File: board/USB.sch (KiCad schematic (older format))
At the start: 47 parts, among them J1 USB_MICRO_B, J7 USB_MICRO_B, P11 CONN_1, P12 CONN_1, P13 CONN_1, U18 USB3340, U2 CY7C68013A_100AC, U24 BDXXGA5WEFJ_, X1 CRYSTAL

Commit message: Issue #1605
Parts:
- added P? (x2): CONN_5, symbol CONN_5
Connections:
- wire segments 176 -> 189
- no-connect marks 5 -> 7
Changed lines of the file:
@@
 Sheet 9 12
 Title "HDMI2USB"
-Date "11 mar 2015"
+Date "12 mar 2015"
 Rev "Rev2"
 Comp ""
@@
 	1    0    0    -1
 $EndComp
-Text Label 14900 3950 0    60   ~ 0
+Text Label 14600 3950 0    60   ~ 0
 CYDP
 Text Label 12000 4050 2    60   ~ 0
@@
 0D 08 60 00 00 34 20 80 01 00 D0 80 00 06 00 40 03 02 18 00 00 0D 08 60 00 00 34 20 80 01 00 D0
 80 00 06 00 40 03 02 18 00 00 0D FE 0D 6E A0 C3 78 63 AE 4C 0B 00 00 00 00 49 45 4E 44 AE 42 60
-82 00 $EndBitmap
+82 06 $EndBitmap
 EndData
 $EndBitmap
-$Comp
-L PWR_FLAG #FLG039
-U 1 1 54AFC1D5
-P 14850 3500
-F 0 "#FLG039" H 14850 3595 30  0001 C CNN
-F 1 "PWR_FLAG" H 14850 3680 30  0000 C CNN
-F 2 "" H 14850 3500 60  0000 C CNN
-F 3 "" H 14850 3500 60  0000 C CNN
-	1    14850 3500
-	1    0    0    -1
-$EndComp
 $Comp
 L USB3340 U18
@@
 Text Label 12000 4150 2    60   ~ 0
 CYDP
-Text Label 14900 3850 0    60   ~ 0
+Text Label 14600 3850 0    60   ~ 0
 CYDN
 Text Label 12400 1450 2    60   ~ 0
@@
 Text Label 3900 8750 2    60   ~ 0
 USB_DM
-Text Label 5350 8800 0    60   ~ 0
+Text Label 5150 8800 0    60   ~ 0
 USB_DP
-Text Label 5350 8900 0    60   ~ 0
+Text Label 5150 8900 0    60   ~ 0
 USB_DM
 NoConn ~ 3500 10500
@@
 	1    0    0    -1
 $EndComp
-Text Label 5350 9000 0    60   ~ 0
+Text Label 5150 9000 0    60   ~ 0
 USB_5V
 $Comp
@@
 Connection ~ 12750 9700
 Wire Wire Line
-	14900 3950 15100 3950
-Wire Wire Line
-	15100 3850 14900 3850
+	14600 3950 15100 3950
+Wire Wire Line
+	14600 3850 15100 3850
 Wire Wire Line
 	14500 6000 14100 6000
@@
 	13250 1650 15350 1650
 Wire Wire Line
-	14850 3500 14850 3750
-Connection ~ 14850 3750
-Wire Wire Line
 	5350 8600 5700 8600
 Wire Wire Line
@@
 Text Notes 12150 8850 0    118  ~ 24
 Cypress CY7C68013A\nDecoupling Capacitors
+$Comp
+L CONN_5 P?
+U 1 1 5501BEC3
+P 15500 3300
+F 0 "P?" V 15450 3300 50  0000 C CNN
+F 1 "CONN_5" V 15550 3300 50  0000 C CNN
+F 2 "" H 15500 3300 60  0000 C CNN
+F 3 "" H 15500 3300 60  0000 C CNN
+	1    15500 3300
+	1    0    0    -1
+$EndComp
+$Comp
+L CONN_5 P?
+U 1 1 5501BED0
+P 6150 9500
+F 0 "P?" V 6100 9500 50  0000 C CNN
+F 1 "CONN_5" V 6200 9500 50  0000 C CNN
+F 2 "" H 6150 9500 60  0000 C CNN
+F 3 "" H 6150 9500 60  0000 C CNN
+	1    6150 9500
+	1    0    0    -1
+$EndComp
+Wire Wire Line
+	5650 9000 5650 9300
+Wire Wire Line
+	5650 9300 5750 9300
+Connection ~ 5650 9000
+Wire Wire Line
+	5600 8900 5600 9400
+Wire Wire Line
+	5600 9400 5750 9400
+Connection ~ 5600 8900
+Wire Wire Line
+	5550 8800 5550 9500
+Wire Wire Line
+	5550 9500 5750 9500
+Connection ~ 5550 8800
+Text Label 5550 9600 0    60   ~ 0
+GND
+Wire Wire Line
+	5550 9600 5750 9600
+NoConn ~ 5750 9700
+NoConn ~ 15100 3500
+Wire Wire Line
+	14750 3750 14750 3100
+Wire Wire Line
+	14750 3100 15100 3100
+Connection ~ 14750 3750
+Text Label 14950 3400 0    60   ~ 0
+GND
+Wire Wire Line
+	14950 3400 15100 3400
+Wire Wire Line
+	15100 3200 14850 3200
+Wire Wire Line
+	14850 3200 14850 3850
+Connection ~ 14850 3850
+Wire Wire Line
+	14900 3950 14900 3300
+Wire Wire Line
+	14900 3300 15100 3300
+Connection ~ 14900 3950
 $EndSCHEMATC

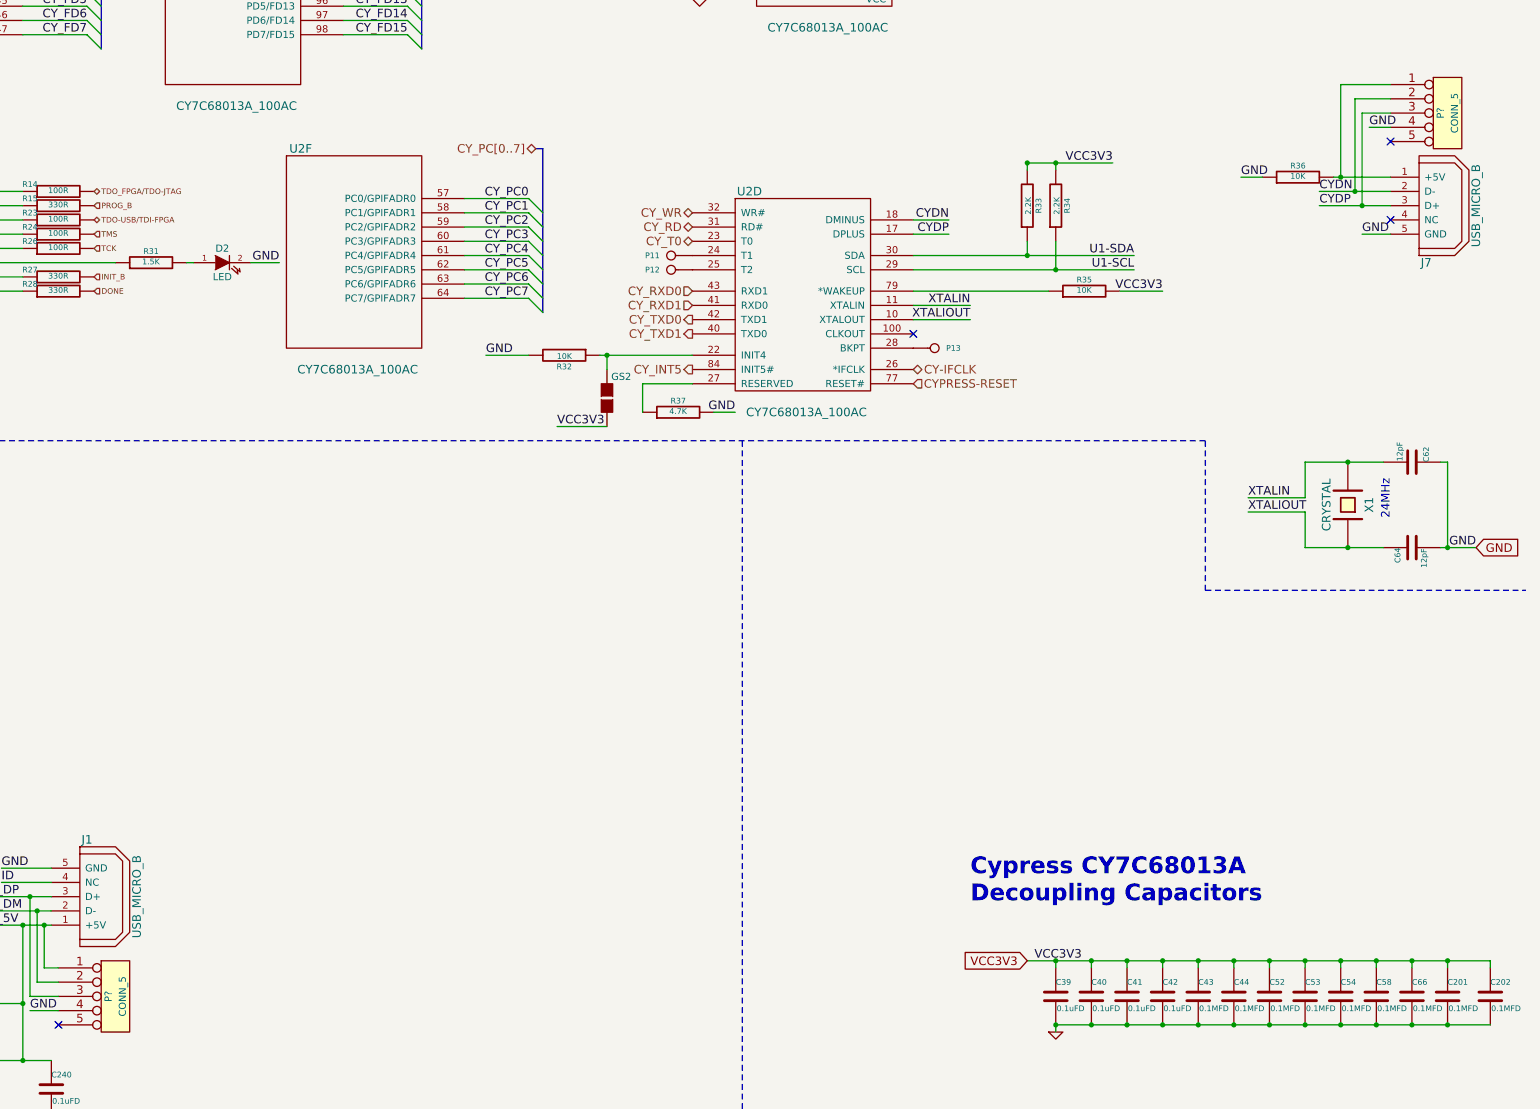
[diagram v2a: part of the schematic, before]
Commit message: Issue #1680 - Bank 0 Ios
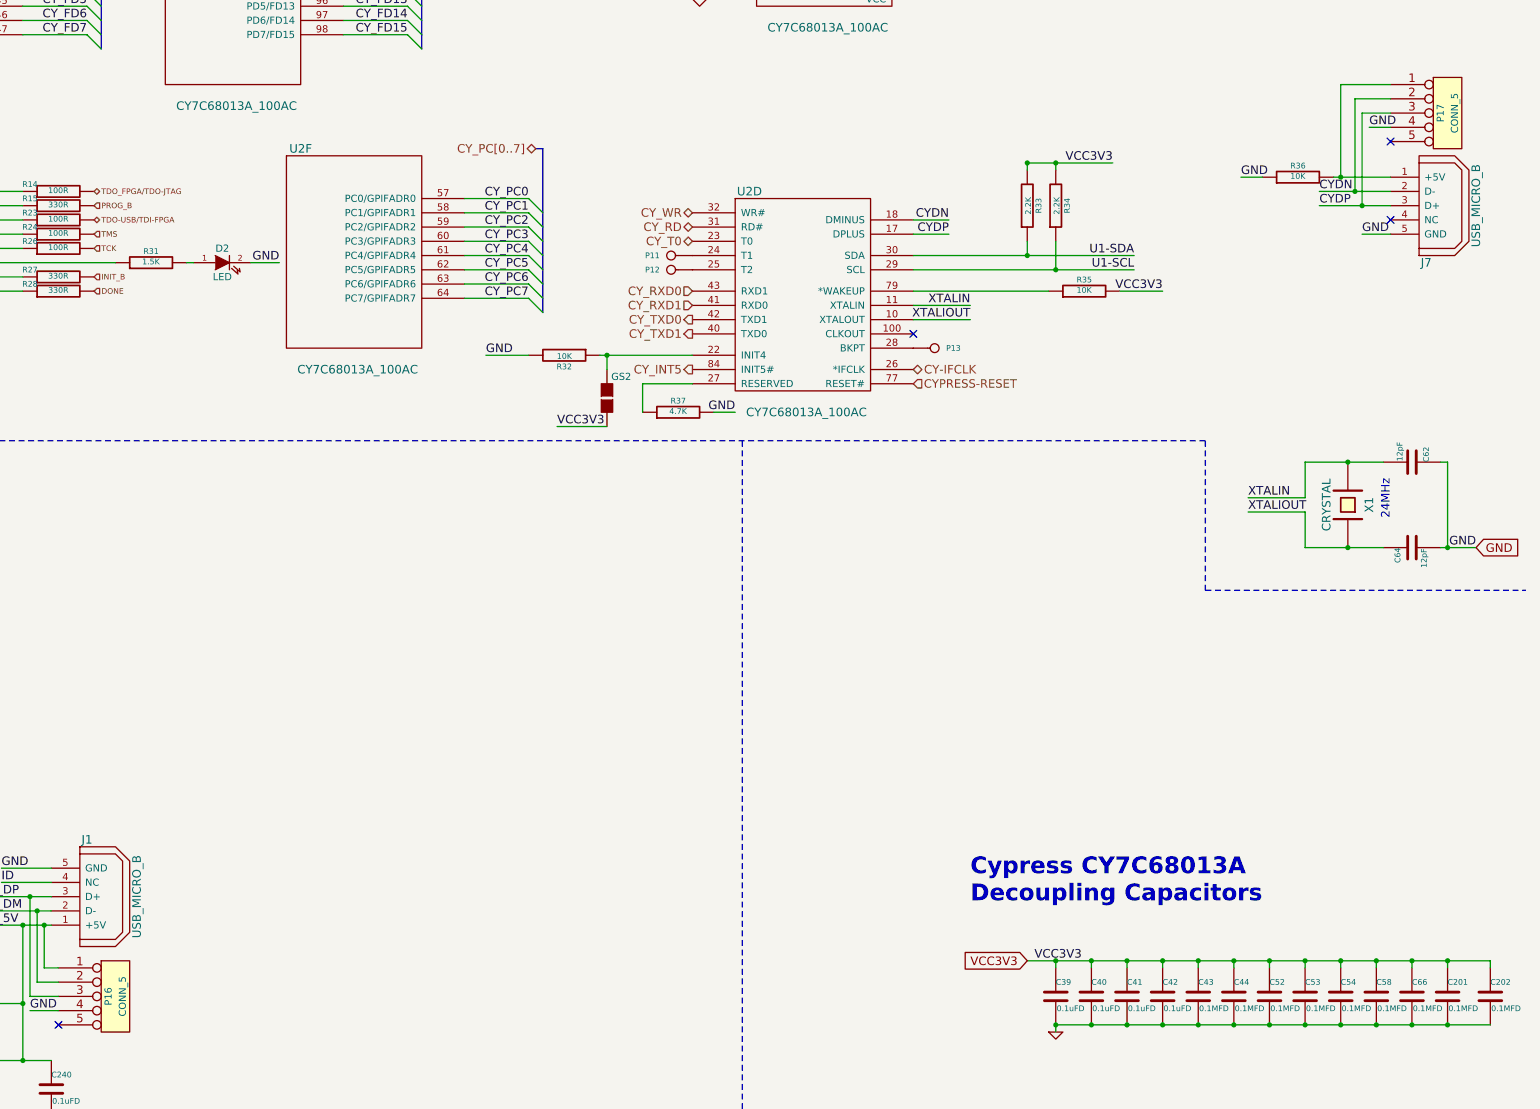
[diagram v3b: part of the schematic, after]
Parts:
- gave numbers to parts that had none: 2
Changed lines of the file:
@@
 $Descr A3 16535 11693
 encoding utf-8
-Sheet 9 12
+Sheet 12 12
 Title "HDMI2USB"
-Date "12 mar 2015"
+Date "23 mar 2015"
 Rev "Rev2"
 Comp ""
@@
 $EndComp
 $Comp
-L GND #PWR038
+L GND #PWR044
 U 1 1 54AFC1CB
 P 12750 9750
-F 0 "#PWR038" H 12750 9750 30  0001 C CNN
+F 0 "#PWR044" H 12750 9750 30  0001 C CNN
 F 1 "GND" H 12750 9680 30  0001 C CNN
 F 2 "" H 12750 9750 60  0000 C CNN
@@
 0D 08 60 00 00 34 20 80 01 00 D0 80 00 06 00 40 03 02 18 00 00 0D 08 60 00 00 34 20 80 01 00 D0
 80 00 06 00 40 03 02 18 00 00 0D FE 0D 6E A0 C3 78 63 AE 4C 0B 00 00 00 00 49 45 4E 44 AE 42 60
-82 06 $EndBitmap
+82 02 $EndBitmap
 EndData
 $EndBitmap
@@
 VCC3V3
 $Comp
-L GND #PWR040
+L GND #PWR045
 U 1 1 54AFC1E5
 P 10250 2500
-F 0 "#PWR040" H 10250 2500 30  0001 C CNN
+F 0 "#PWR045" H 10250 2500 30  0001 C CNN
 F 1 "GND" H 10250 2430 30  0001 C CNN
 F 2 "" H 10250 2500 60  0000 C CNN
@@
 USB_5V
 $Comp
-L GND #PWR041
+L GND #PWR046
 U 1 1 54E5E8EF
 P 2500 11000
-F 0 "#PWR041" H 2500 11000 30  0001 C CNN
+F 0 "#PWR046" H 2500 11000 30  0001 C CNN
 F 1 "GND" H 2500 10930 30  0001 C CNN
 F 2 "" H 2500 11000 60  0000 C CNN
@@
 Cypress CY7C68013A\nDecoupling Capacitors
 $Comp
-L CONN_5 P?
+L CONN_5 P17
 U 1 1 5501BEC3
 P 15500 3300
-F 0 "P?" V 15450 3300 50  0000 C CNN
+F 0 "P17" V 15450 3300 50  0000 C CNN
 F 1 "CONN_5" V 15550 3300 50  0000 C CNN
 F 2 "" H 15500 3300 60  0000 C CNN
@@
 $EndComp
 $Comp
-L CONN_5 P?
+L CONN_5 P16
 U 1 1 5501BED0
 P 6150 9500
-F 0 "P?" V 6100 9500 50  0000 C CNN
+F 0 "P16" V 6100 9500 50  0000 C CNN
 F 1 "CONN_5" V 6200 9500 50  0000 C CNN
 F 2 "" H 6150 9500 60  0000 C CNN

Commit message: Issue #1683
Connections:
- net U1-SCL renamed MAC_SCL
- net U1-SDA renamed MAC_SDA
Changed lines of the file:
@@
 $Descr A3 16535 11693
 encoding utf-8
-Sheet 12 12
+Sheet 11 12
 Title "HDMI2USB"
-Date "23 mar 2015"
+Date "25 mar 2015"
 Rev "Rev2"
 Comp ""
@@
 $EndComp
 $Comp
-L GND #PWR044
+L GND #PWR040
 U 1 1 54AFC1CB
 P 12750 9750
-F 0 "#PWR044" H 12750 9750 30  0001 C CNN
+F 0 "#PWR040" H 12750 9750 30  0001 C CNN
 F 1 "GND" H 12750 9680 30  0001 C CNN
 F 2 "" H 12750 9750 60  0000 C CNN
@@
 0D 08 60 00 00 34 20 80 01 00 D0 80 00 06 00 40 03 02 18 00 00 0D 08 60 00 00 34 20 80 01 00 D0
 80 00 06 00 40 03 02 18 00 00 0D FE 0D 6E A0 C3 78 63 AE 4C 0B 00 00 00 00 49 45 4E 44 AE 42 60
-82 02 $EndBitmap
+82 00 $EndBitmap
 EndData
 $EndBitmap
@@
 VCC3V3
 $Comp
-L GND #PWR045
+L GND #PWR041
 U 1 1 54AFC1E5
 P 10250 2500
-F 0 "#PWR045" H 10250 2500 30  0001 C CNN
+F 0 "#PWR041" H 10250 2500 30  0001 C CNN
 F 1 "GND" H 10250 2430 30  0001 C CNN
 F 2 "" H 10250 2500 60  0000 C CNN
@@
 USB_5V
 $Comp
-L GND #PWR046
+L GND #PWR042
 U 1 1 54E5E8EF
 P 2500 11000
-F 0 "#PWR046" H 2500 11000 30  0001 C CNN
+F 0 "#PWR042" H 2500 11000 30  0001 C CNN
 F 1 "GND" H 2500 10930 30  0001 C CNN
 F 2 "" H 2500 11000 60  0000 C CNN
@@
 	14900 3300 15100 3300
 Connection ~ 14900 3950
+Text HLabel 13300 4300 2    39   BiDi ~ 0
+MAC_SDA
+Text HLabel 13300 4400 2    39   Input ~ 0
+MAC_SCL
 $EndSCHEMATC

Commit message: Issue #1670
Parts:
- added P18: CONN_2, symbol CONN_2
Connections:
- net MAC_SDA: now also P18.2 (PM); no longer R33.1, U2.30 (SDA)
- new net U1-SDA: P18.1 (P1), R33.1, U2.30 (SDA)
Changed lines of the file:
@@
 $Descr A3 16535 11693
 encoding utf-8
-Sheet 11 12
+Sheet 10 12
 Title "HDMI2USB"
-Date "25 mar 2015"
+Date "30 mar 2015"
 Rev "Rev2"
 Comp ""
@@
 0D 08 60 00 00 34 20 80 01 00 D0 80 00 06 00 40 03 02 18 00 00 0D 08 60 00 00 34 20 80 01 00 D0
 80 00 06 00 40 03 02 18 00 00 0D FE 0D 6E A0 C3 78 63 AE 4C 0B 00 00 00 00 49 45 4E 44 AE 42 60
-82 00 $EndBitmap
+82 0E $EndBitmap
 EndData
 $EndBitmap
@@
 Text Notes 650  850  0    118  ~ 24
 USB 2.0 Device Port\nJTAG Programmer and "Easy" High Speed USB 2.0 Interface\nCypress FX2 based
+Text Notes 12150 8850 0    118  ~ 24
+Cypress CY7C68013A\nDecoupling Capacitors
+$Comp
+L CONN_5 P17
+U 1 1 5501BEC3
+P 15500 3300
+F 0 "P17" V 15450 3300 50  0000 C CNN
+F 1 "CONN_5" V 15550 3300 50  0000 C CNN
+F 2 "" H 15500 3300 60  0000 C CNN
+F 3 "" H 15500 3300 60  0000 C CNN
+	1    15500 3300
+	1    0    0    -1
+$EndComp
+$Comp
+L CONN_5 P16
+U 1 1 5501BED0
+P 6150 9500
+F 0 "P16" V 6100 9500 50  0000 C CNN
+F 1 "CONN_5" V 6200 9500 50  0000 C CNN
+F 2 "" H 6150 9500 60  0000 C CNN
+F 3 "" H 6150 9500 60  0000 C CNN
+	1    6150 9500
+	1    0    0    -1
+$EndComp
+Text Label 5550 9600 0    60   ~ 0
+GND
+NoConn ~ 5750 9700
+NoConn ~ 15100 3500
+Text Label 14950 3400 0    60   ~ 0
+GND
+Text HLabel 13650 4300 2    39   BiDi ~ 0
+MAC_SDA
+Text HLabel 13300 4400 2    39   Input ~ 0
+MAC_SCL
 Wire Wire Line
 	14500 9250 14500 9300
@@
 Connection ~ 15500 6350
 Connection ~ 14500 9700
-Wire Wire Line
-	11750 4300 13300 4300
 Wire Wire Line
 	11750 4400 13300 4400
@@
 Wire Notes Line
 	10550 5600 10550 11200
-Text Notes 12150 8850 0    118  ~ 24
-Cypress CY7C68013A\nDecoupling Capacitors
-$Comp
-L CONN_5 P17
-U 1 1 5501BEC3
-P 15500 3300
-F 0 "P17" V 15450 3300 50  0000 C CNN
-F 1 "CONN_5" V 15550 3300 50  0000 C CNN
-F 2 "" H 15500 3300 60  0000 C CNN
-F 3 "" H 15500 3300 60  0000 C CNN
-	1    15500 3300
-	1    0    0    -1
-$EndComp
-$Comp
-L CONN_5 P16
-U 1 1 5501BED0
-P 6150 9500
-F 0 "P16" V 6100 9500 50  0000 C CNN
-F 1 "CONN_5" V 6200 9500 50  0000 C CNN
-F 2 "" H 6150 9500 60  0000 C CNN
-F 3 "" H 6150 9500 60  0000 C CNN
-	1    6150 9500
-	1    0    0    -1
-$EndComp
 Wire Wire Line
 	5650 9000 5650 9300
@@
 	5550 9500 5750 9500
 Connection ~ 5550 8800
-Text Label 5550 9600 0    60   ~ 0
-GND
 Wire Wire Line
 	5550 9600 5750 9600
-NoConn ~ 5750 9700
-NoConn ~ 15100 3500
 Wire Wire Line
 	14750 3750 14750 3100
@@
 	14750 3100 15100 3100
 Connection ~ 14750 3750
-Text Label 14950 3400 0    60   ~ 0
-GND
 Wire Wire Line
 	14950 3400 15100 3400
@@
 	14900 3300 15100 3300
 Connection ~ 14900 3950
-Text HLabel 13300 4300 2    39   BiDi ~ 0
-MAC_SDA
-Text HLabel 13300 4400 2    39   Input ~ 0
-MAC_SCL
+Wire Wire Line
+	11750 4300 13300 4300
+$Comp
+L CONN_2 P18
+U 1 1 551B9FE1
+P 13400 3950
+F 0 "P18" V 13350 3950 40  0000 C CNN
+F 1 "CONN_2" V 13450 3950 40  0000 C CNN
+F 2 "" H 13400 3950 60  0000 C CNN
+F 3 "" H 13400 3950 60  0000 C CNN
+	1    13400 3950
+	0    -1   -1   0
+$EndComp
+Wire Wire Line
+	13500 4300 13650 4300
 $EndSCHEMATC

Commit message: Issue #1585
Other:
- note added: "Cypress EEPROM disable"
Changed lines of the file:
@@
 LIBS:contrib
 LIBS:valves
-LIBS:hdmi2usb
-LIBS:timvideos-pcie-8x
 LIBS:HDMI2USB-cache
 EELAYER 27 0
@@
 Sheet 10 12
 Title "HDMI2USB"
-Date "30 mar 2015"
+Date "1 apr 2015"
 Rev "Rev2"
 Comp ""
@@
 $EndComp
 $Comp
-L GND #PWR42
+L GND #PWR044
 U 1 1 54AFC1CB
 P 12750 9750
-F 0 "#PWR42" H 12750 9750 30  0001 C CNN
+F 0 "#PWR044" H 12750 9750 30  0001 C CNN
 F 1 "GND" H 12750 9680 30  0001 C CNN
 F 2 "" H 12750 9750 60  0000 C CNN
@@
 0D 08 60 00 00 34 20 80 01 00 D0 80 00 06 00 40 03 02 18 00 00 0D 08 60 00 00 34 20 80 01 00 D0
 80 00 06 00 40 03 02 18 00 00 0D FE 0D 6E A0 C3 78 63 AE 4C 0B 00 00 00 00 49 45 4E 44 AE 42 60
-82 08 $EndBitmap
+82 00 $EndBitmap
 EndData
 $EndBitmap
@@
 VCC3V3
 $Comp
-L GND #PWR41
+L GND #PWR045
 U 1 1 54AFC1E5
 P 10250 2500
-F 0 "#PWR41" H 10250 2500 30  0001 C CNN
+F 0 "#PWR045" H 10250 2500 30  0001 C CNN
 F 1 "GND" H 10250 2430 30  0001 C CNN
 F 2 "" H 10250 2500 60  0000 C CNN
@@
 USB_5V
 $Comp
-L GND #PWR40
+L GND #PWR046
 U 1 1 54E5E8EF
 P 2500 11000
-F 0 "#PWR40" H 2500 11000 30  0001 C CNN
+F 0 "#PWR046" H 2500 11000 30  0001 C CNN
 F 1 "GND" H 2500 10930 30  0001 C CNN
 F 2 "" H 2500 11000 60  0000 C CNN
@@
 Wire Wire Line
 	13500 4300 13650 4300
+Text Notes 13150 3750 0    39   ~ 0
+Cypress EEPROM disable
 $EndSCHEMATC
